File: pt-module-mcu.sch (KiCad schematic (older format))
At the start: 22 parts

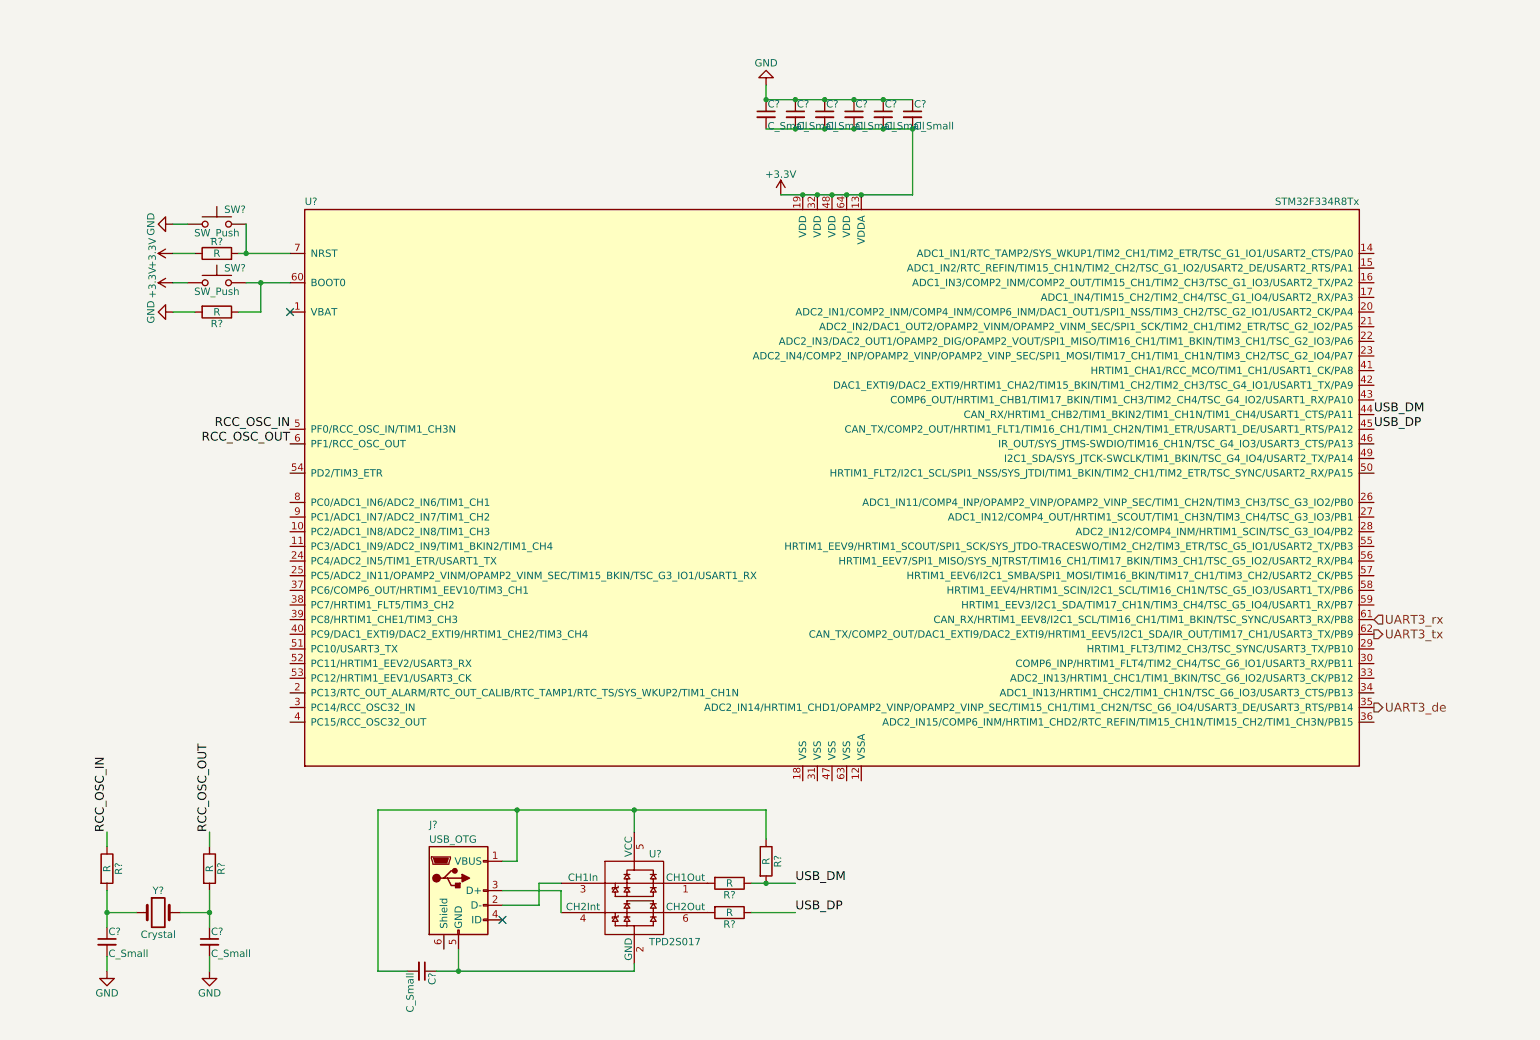
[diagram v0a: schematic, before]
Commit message: Added USB to UART interface
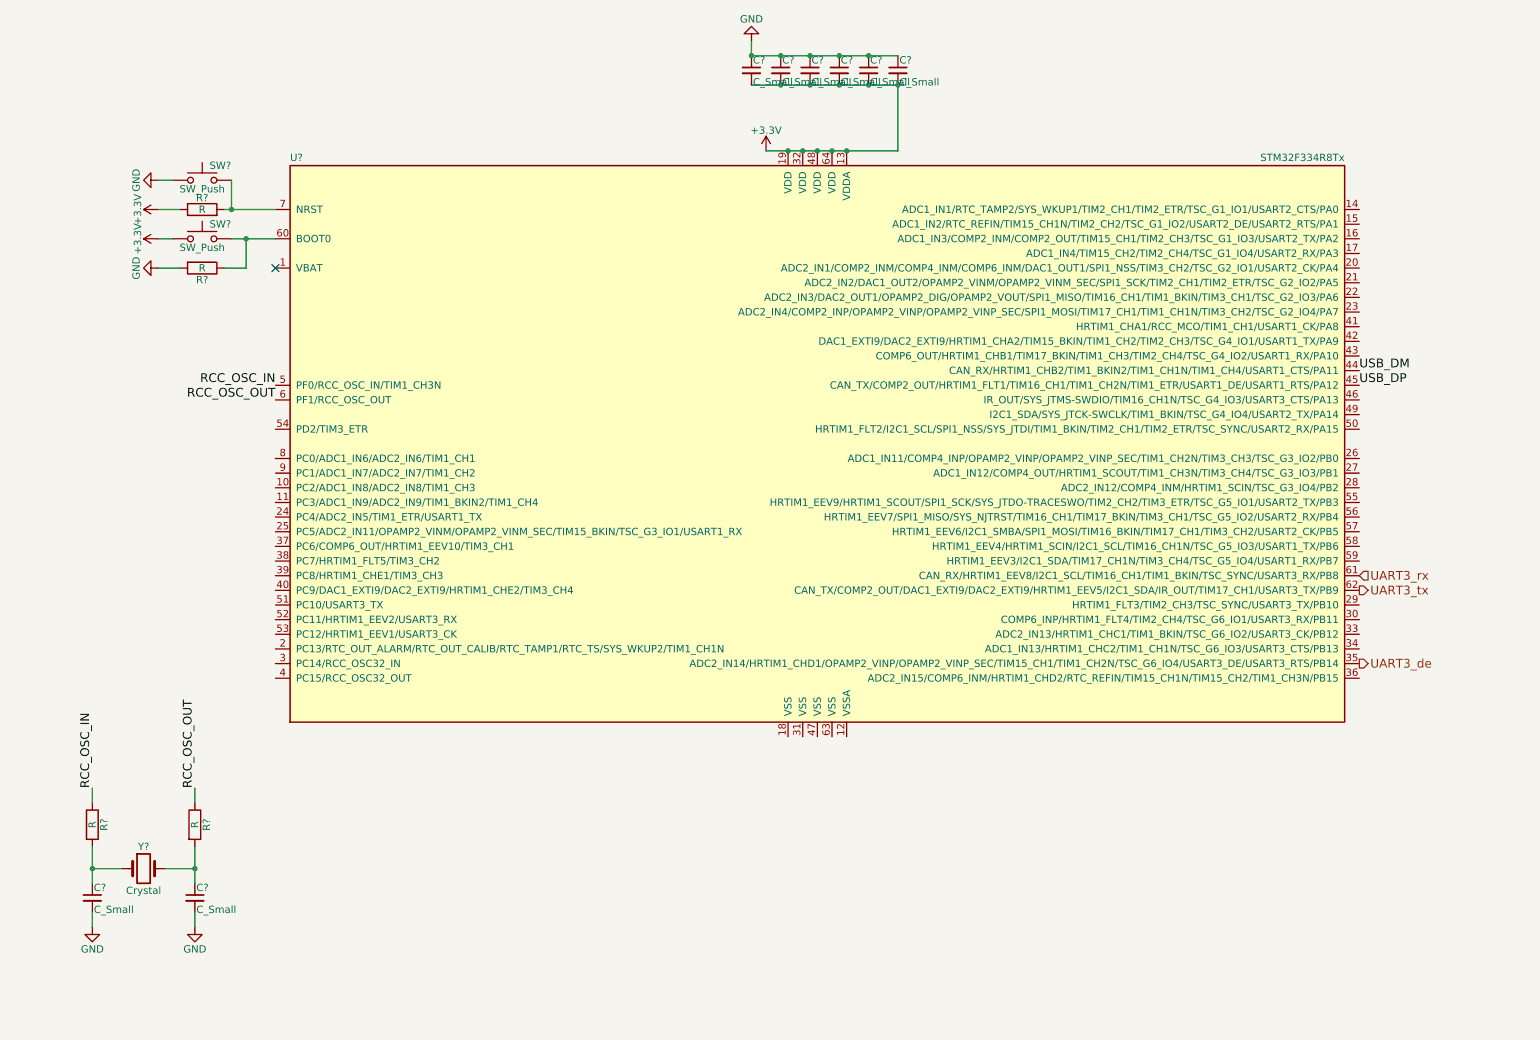
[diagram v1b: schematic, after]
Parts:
- removed C?: C_Small, symbol C_Small
- removed J?: USB_OTG, symbol USB_OTG
- removed R? (x3): R, symbol R
- removed U?: TPD2S017, symbol TPD2S017
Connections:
- no-connect marks 2 -> 1
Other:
- moved on the sheet: C?, R?, SW?, U?, Y?

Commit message: Added USB UART hierarchical connection
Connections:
- net UART1_TX: now reaches U?.58 (HRTIM1_EEV4/HRTIM1_SCIN/I2C1_SCL/TIM16_CH1N/TSC_G5_IO3/USART1_TX/PB6)
- net UART1_RX: now reaches U?.59 (HRTIM1_EEV3/I2C1_SDA/TIM17_CH1N/TIM3_CH4/TSC_G5_IO4/USART1_RX/PB7)
- net USB_DM renamed UART1_CTS
- net USB_DP renamed UART1_RTS
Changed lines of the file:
@@
 Text HLabel 9950 5150 2    60   Output ~ 0
 UART3_de
-Text Label 9950 3150 0    60   ~ 0
-USB_DM
-Text Label 9950 3250 0    60   ~ 0
-USB_DP
 Connection ~ 6050 1650
 Wire Wire Line
@@
 Connection ~ 5800 1000
 Connection ~ 6800 1200
+Text HLabel 9950 4350 2    60   Input ~ 0
+UART1_TX
+Text HLabel 9950 4450 2    60   Input ~ 0
+UART1_RX
+Text HLabel 9950 3150 2    60   Input ~ 0
+UART1_CTS
+Text HLabel 9950 3250 2    60   Input ~ 0
+UART1_RTS
 $EndSCHEMATC

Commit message: Added another rs485 link to MCU
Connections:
- net UART2_de: now reaches U?.15 (ADC1_IN2/RTC_REFIN/TIM15_CH1N/TIM2_CH2/TSC_G1_IO2/USART2_DE/USART2_RTS/PA1)
- net UART2_TX: now reaches U?.16 (ADC1_IN3/COMP2_INM/COMP2_OUT/TIM15_CH1/TIM2_CH3/TSC_G1_IO3/USART2_TX/PA2)
- net UART2_RX: now reaches U?.17 (ADC1_IN4/TIM15_CH2/TIM2_CH4/TSC_G1_IO4/USART2_RX/PA3)
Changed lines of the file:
@@
 Text HLabel 9950 3250 2    60   Input ~ 0
 UART1_RTS
+Text HLabel 9950 2350 2    60   Input ~ 0
+UART2_RX
+Text HLabel 9950 2250 2    60   Input ~ 0
+UART2_TX
+Text HLabel 9950 2150 2    60   Output ~ 0
+UART2_de
 $EndSCHEMATC

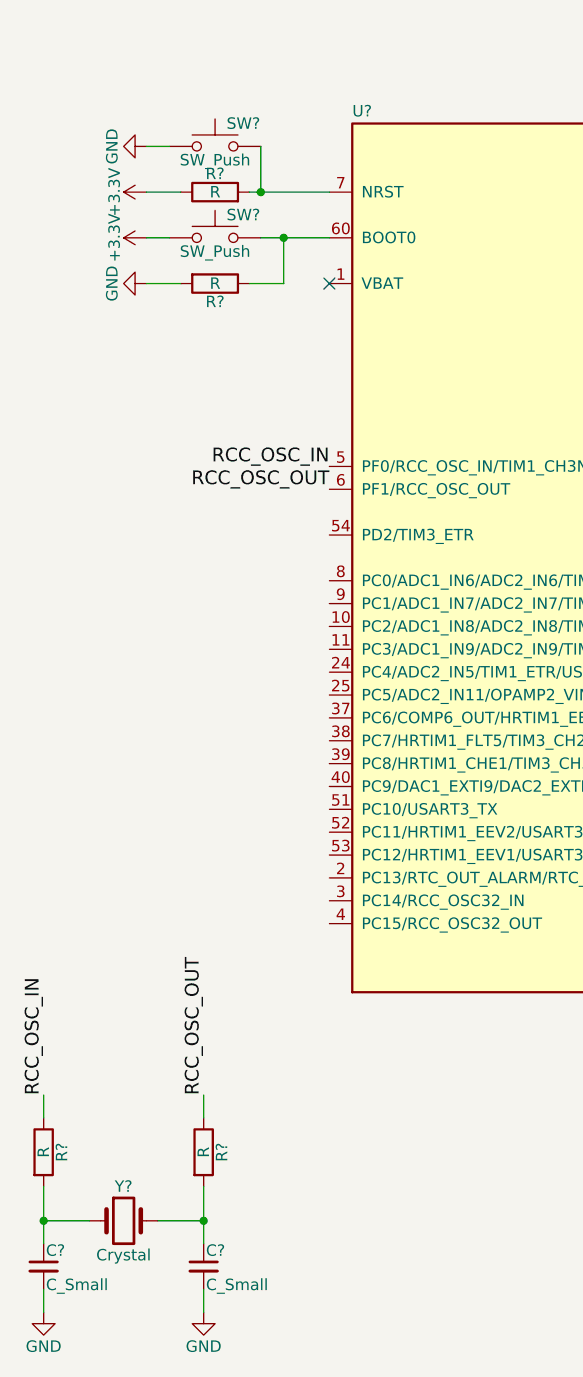
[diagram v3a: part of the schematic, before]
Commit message: Added resistor and capacitor values in MCU sheet.
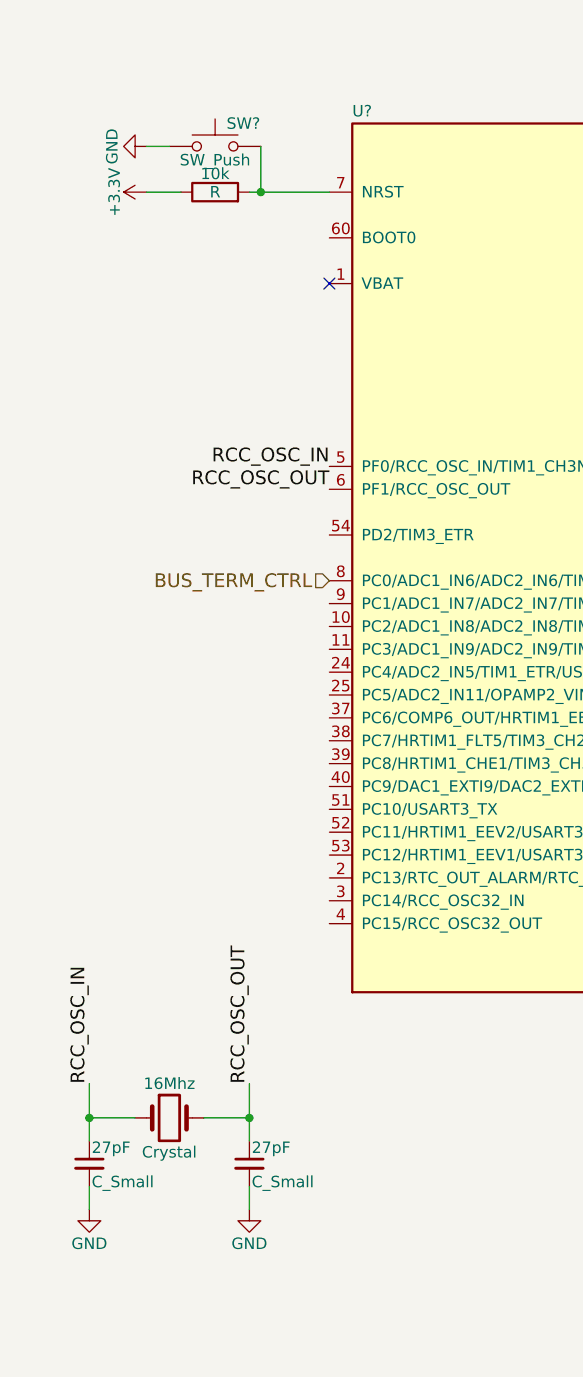
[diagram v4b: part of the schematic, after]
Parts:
- removed R? (x3): R, symbol R
- removed SW?: SW_Push, symbol SW_Push
- gave numbers to parts that had none: 3
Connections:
- net RCC_OSC_IN: now also 16Mhz.1, 27pF.1
- net RCC_OSC_OUT: now also 16Mhz.2, 27pF.1
- net BUS_TERM_CTRL: now reaches U?.8 (PC0/ADC1_IN6/ADC2_IN6/TIM1_CH1)
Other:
- moved on the sheet: 16Mhz, 27pF
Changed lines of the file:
@@
 $EndComp
 $Comp
-L Crystal Y?
+L Crystal 16Mhz
 U 1 1 597ECED5
-P 1650 6550
-F 0 "Y?" H 1650 6700 50  0000 C CNN
-F 1 "Crystal" H 1650 6400 50  0000 C CNN
-F 2 "" H 1650 6550 50  0001 C CNN
-F 3 "" H 1650 6550 50  0001 C CNN
-	1    1650 6550
-	1    0    0    -1
-$EndComp
-$Comp
-L C_Small C?
+P 1850 6100
+F 0 "16Mhz" H 1850 6250 50  0000 C CNN
+F 1 "Crystal" H 1850 5950 50  0000 C CNN
+F 2 "" H 1850 6100 50  0001 C CNN
+F 3 "" H 1850 6100 50  0001 C CNN
+	1    1850 6100
+	1    0    0    -1
+$EndComp
+$Comp
+L C_Small 27pF
 U 1 1 597ECFD6
-P 1300 6750
-F 0 "C?" H 1310 6820 50  0000 L CNN
-F 1 "C_Small" H 1310 6670 50  0000 L CNN
-F 2 "" H 1300 6750 50  0001 C CNN
-F 3 "" H 1300 6750 50  0001 C CNN
-	1    1300 6750
-	1    0    0    -1
-$EndComp
-$Comp
-L C_Small C?
+P 1500 6300
+F 0 "27pF" H 1510 6370 50  0000 L CNN
+F 1 "C_Small" H 1510 6220 50  0000 L CNN
+F 2 "" H 1500 6300 50  0001 C CNN
+F 3 "" H 1500 6300 50  0001 C CNN
+	1    1500 6300
+	1    0    0    -1
+$EndComp
+$Comp
+L C_Small 27pF
 U 1 1 597ED20D
-P 2000 6750
-F 0 "C?" H 2010 6820 50  0000 L CNN
-F 1 "C_Small" H 2010 6670 50  0000 L CNN
-F 2 "" H 2000 6750 50  0001 C CNN
-F 3 "" H 2000 6750 50  0001 C CNN
-	1    2000 6750
+P 2200 6300
+F 0 "27pF" H 2210 6370 50  0000 L CNN
+F 1 "C_Small" H 2210 6220 50  0000 L CNN
+F 2 "" H 2200 6300 50  0001 C CNN
+F 3 "" H 2200 6300 50  0001 C CNN
+	1    2200 6300
 	1    0    0    -1
 $EndComp
@@
 L GND #PWR016
 U 1 1 597EDE48
-P 1300 6950
-F 0 "#PWR016" H 1300 6700 50  0001 C CNN
-F 1 "GND" H 1300 6800 50  0000 C CNN
-F 2 "" H 1300 6950 50  0001 C CNN
-F 3 "" H 1300 6950 50  0001 C CNN
-	1    1300 6950
+P 1500 6500
+F 0 "#PWR016" H 1500 6250 50  0001 C CNN
+F 1 "GND" H 1500 6350 50  0000 C CNN
+F 2 "" H 1500 6500 50  0001 C CNN
+F 3 "" H 1500 6500 50  0001 C CNN
+	1    1500 6500
 	1    0    0    -1
 $EndComp
@@
 L GND #PWR017
 U 1 1 597EDE64
-P 2000 6950
-F 0 "#PWR017" H 2000 6700 50  0001 C CNN
-F 1 "GND" H 2000 6800 50  0000 C CNN
-F 2 "" H 2000 6950 50  0001 C CNN
-F 3 "" H 2000 6950 50  0001 C CNN
-	1    2000 6950
-	1    0    0    -1
-$EndComp
-$Comp
-L R R?
-U 1 1 597EE298
-P 2000 6250
-F 0 "R?" V 2080 6250 50  0000 C CNN
-F 1 "R" V 2000 6250 50  0000 C CNN
-F 2 "" V 1930 6250 50  0001 C CNN
-F 3 "" H 2000 6250 50  0001 C CNN
-	1    2000 6250
-	1    0    0    -1
-$EndComp
-$Comp
-L R R?
-U 1 1 597EE36F
-P 1300 6250
-F 0 "R?" V 1380 6250 50  0000 C CNN
-F 1 "R" V 1300 6250 50  0000 C CNN
-F 2 "" V 1230 6250 50  0001 C CNN
-F 3 "" H 1300 6250 50  0001 C CNN
-	1    1300 6250
-	1    0    0    -1
-$EndComp
-Text Label 2000 6000 1    60   ~ 0
+P 2200 6500
+F 0 "#PWR017" H 2200 6250 50  0001 C CNN
+F 1 "GND" H 2200 6350 50  0000 C CNN
+F 2 "" H 2200 6500 50  0001 C CNN
+F 3 "" H 2200 6500 50  0001 C CNN
+	1    2200 6500
+	1    0    0    -1
+$EndComp
+Text Label 2200 5950 1    60   ~ 0
 RCC_OSC_OUT
-Text Label 1300 6000 1    60   ~ 0
+Text Label 1500 5950 1    60   ~ 0
 RCC_OSC_IN
 $Comp
-L R R?
-U 1 1 597EF512
-P 2050 2450
-F 0 "R?" V 2130 2450 50  0000 C CNN
-F 1 "R" V 2050 2450 50  0000 C CNN
-F 2 "" V 1980 2450 50  0001 C CNN
-F 3 "" H 2050 2450 50  0001 C CNN
-	1    2050 2450
-	0    1    1    0
-$EndComp
-$Comp
-L SW_Push SW?
-U 1 1 597EF5BF
-P 2050 2250
-F 0 "SW?" H 2100 2350 50  0000 L CNN
-F 1 "SW_Push" H 2050 2190 50  0000 C CNN
-F 2 "" H 2050 2450 50  0001 C CNN
-F 3 "" H 2050 2450 50  0001 C CNN
-	1    2050 2250
-	1    0    0    -1
-$EndComp
-$Comp
-L GND #PWR018
-U 1 1 597EF6EE
-P 1750 2450
-F 0 "#PWR018" H 1750 2200 50  0001 C CNN
-F 1 "GND" H 1750 2300 50  0000 C CNN
-F 2 "" H 1750 2450 50  0001 C CNN
-F 3 "" H 1750 2450 50  0001 C CNN
-	1    1750 2450
-	0    1    1    0
-$EndComp
-$Comp
-L R R?
+L R 10k
 U 1 1 597EF7C5
 P 2050 2050
-F 0 "R?" V 2130 2050 50  0000 C CNN
+F 0 "10k" V 2130 2050 50  0000 C CNN
 F 1 "R" V 2050 2050 50  0000 C CNN
 F 2 "" V 1980 2050 50  0001 C CNN
@@
 	0    -1   -1   0
 $EndComp
-$Comp
-L +3.3V #PWR025
-U 1 1 5980CC78
-P 1750 2250
-F 0 "#PWR025" H 1750 2100 50  0001 C CNN
-F 1 "+3.3V" H 1750 2390 50  0000 C CNN
-F 2 "" H 1750 2250 50  0001 C CNN
-F 3 "" H 1750 2250 50  0001 C CNN
-	1    1750 2250
-	0    -1   -1   0
-$EndComp
 Text HLabel 9950 4650 2    60   Output ~ 0
 UART3_tx
@@
 Connection ~ 6050 1650
 Wire Wire Line
-	1850 2250 1750 2250
-Wire Wire Line
 	1900 2050 1750 2050
 Wire Wire Line
@@
 Wire Wire Line
 	2200 2050 2550 2050
-Wire Wire Line
-	1750 2450 1900 2450
-Connection ~ 2350 2250
-Wire Wire Line
-	2350 2450 2350 2250
-Wire Wire Line
-	2200 2450 2350 2450
-Wire Wire Line
-	2550 2250 2250 2250
-Wire Wire Line
-	1300 6100 1300 6000
-Wire Wire Line
-	2000 6100 2000 6000
-Connection ~ 2000 6550
-Connection ~ 1300 6550
-Wire Wire Line
-	1300 6850 1300 6950
-Wire Wire Line
-	2000 6850 2000 6950
-Wire Wire Line
-	1300 6400 1300 6650
-Wire Wire Line
-	1500 6550 1300 6550
-Wire Wire Line
-	2000 6400 2000 6650
-Wire Wire Line
-	1800 6550 2000 6550
+Connection ~ 2200 6100
+Connection ~ 1500 6100
+Wire Wire Line
+	1500 6400 1500 6500
+Wire Wire Line
+	2200 6400 2200 6500
+Wire Wire Line
+	1500 5950 1500 6200
+Wire Wire Line
+	1700 6100 1500 6100
+Wire Wire Line
+	2200 5950 2200 6200
+Wire Wire Line
+	2000 6100 2200 6100
 Wire Wire Line
 	5900 1650 6800 1650
@@
 Text HLabel 9950 2150 2    60   Output ~ 0
 UART2_de
+Text HLabel 2550 3750 0    60   Input ~ 0
+BUS_TERM_CTRL
 $EndSCHEMATC
